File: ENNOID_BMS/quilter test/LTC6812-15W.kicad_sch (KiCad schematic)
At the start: 153 parts, among them J1 PB MB 2, J10 PB MB 1, J11 PA MA 1, J2 PA MA 2, J3 Sensors, J5 Cells, J6 Sensors, Q1 DZTT5551, Q17 DZTT5551, Q18 2N7002, Q19 2N7002, Q20 2N7002, Q21 2N7002, Q22 2N7002, Q23 2N7002, Q24 2N7002, Q25 2N7002, Q26 2N7002, Q27 2N7002, Q28 2N7002, Q29 2N7002, Q30 2N7002, Q31 2N7002, Q32 2N7002, U1 LTC6812-1, U2 LTC6812-1

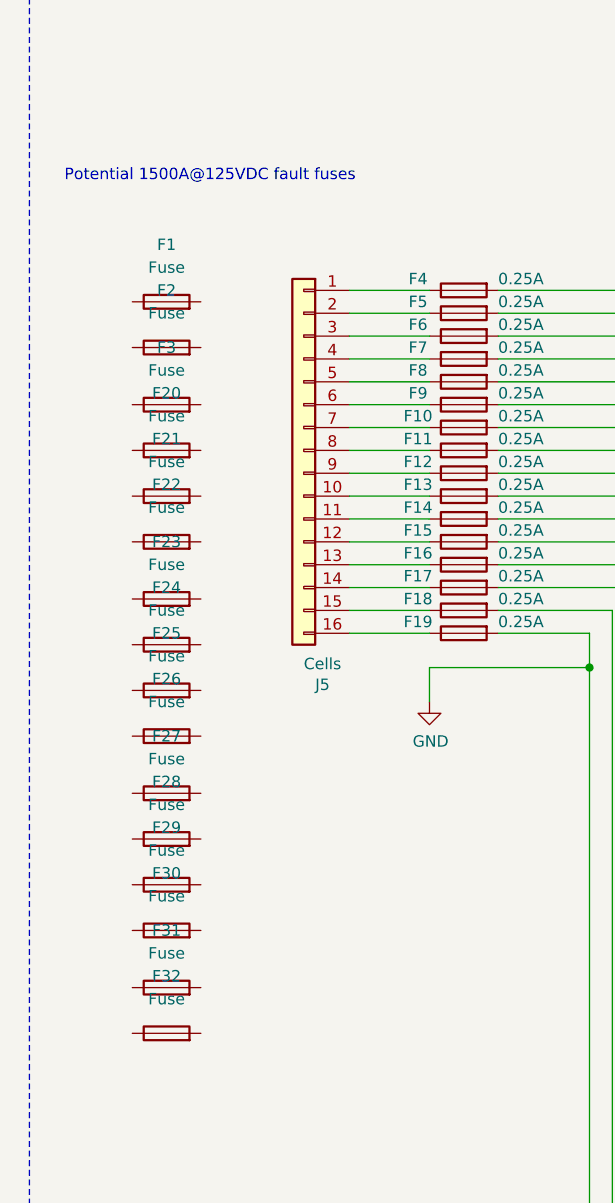
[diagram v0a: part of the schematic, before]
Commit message: slave with new fuses added
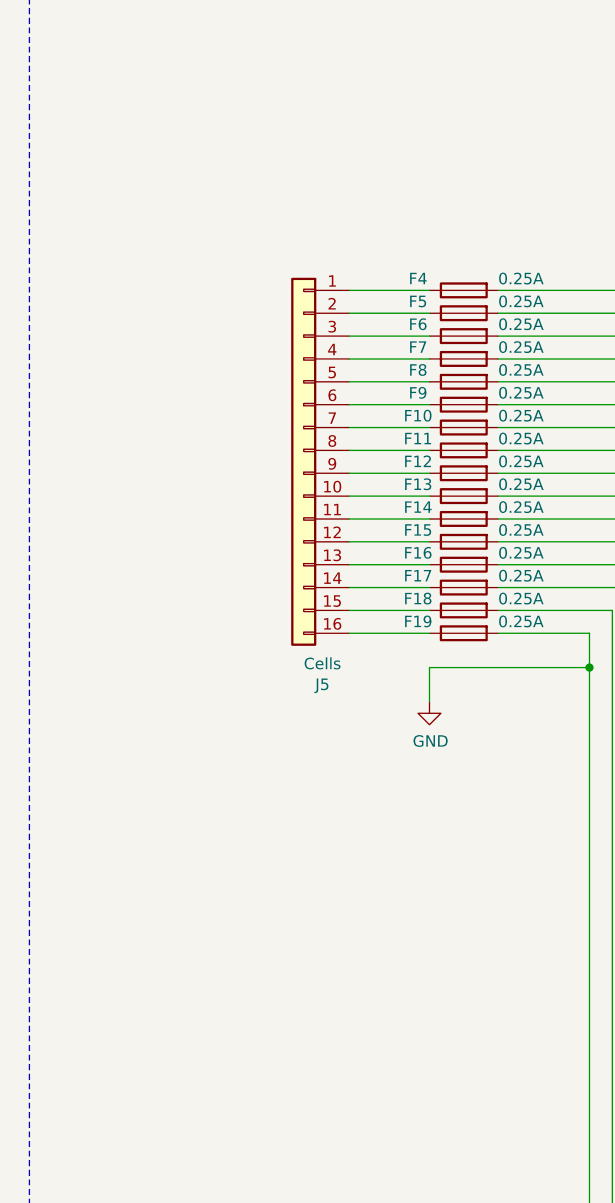
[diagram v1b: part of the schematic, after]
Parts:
- removed F1, F2, F20, F21, F22, F23, F24, F25, F26, F27, F28, F29, F3, F30, F31, F32: Fuse, ENNOID:FUSC10948X488N, symbol Device:Fuse
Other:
- note removed: "Potential 1500A@125VDC fault fuses"
